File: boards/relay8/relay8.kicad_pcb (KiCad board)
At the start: 2 copper layers, 150 x 95 mm, 56 parts, among them J1 USB-C, J11 CH1, J12 CH2, J13 CH3, J14 CH4, J15 CH5, J16 CH6, J17 CH7, J18 CH8, J2 UART, J3 5V DC 2A, K1 SRD-05VDC-SL-C, K2 SRD-05VDC-SL-C, K3 SRD-05VDC-SL-C, K4 SRD-05VDC-SL-C, K5 SRD-05VDC-SL-C, K6 SRD-05VDC-SL-C, K7 SRD-05VDC-SL-C, K8 SRD-05VDC-SL-C, SW1 RESET, SW2 BOOT, U1 ESP32-C3-WROOM-02-N4, U2 AP2112K-3.3, U3 ULN2803A

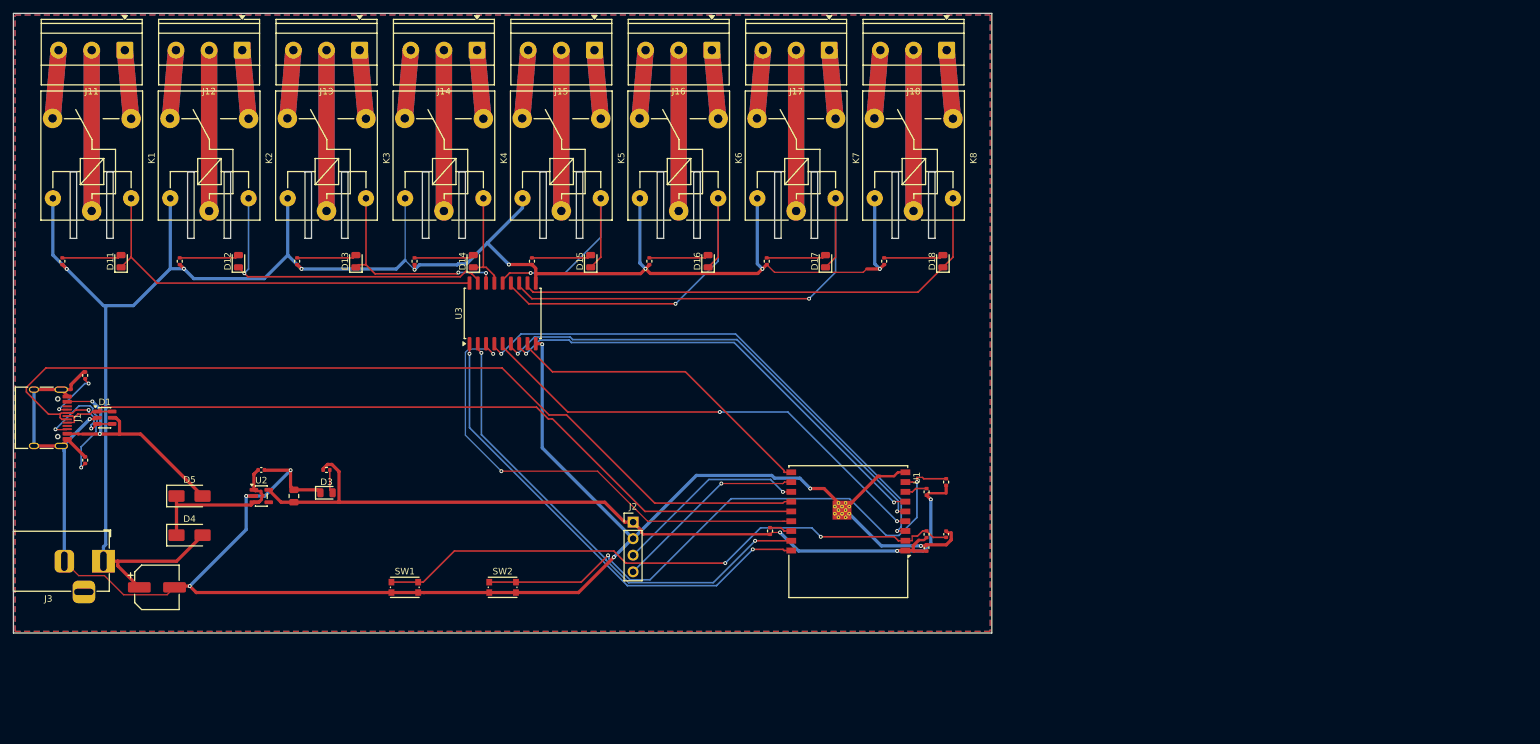
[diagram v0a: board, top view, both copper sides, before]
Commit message: relay8: print NC / COM / NO under every terminal block
The wiring doc said the terminals were labelled, but the board had no
such silkscreen; the only way to tell the contacts apart was the doc.
Each label is generated from the net its pad is on (RL3_NO -> "NO"), so
it cannot disagree with the circuit. Relays, indicator LEDs and the
ULN2803 move down 2.5 mm to make room; the terminal references move to
F.Fab. The 8 silk_overlap warnings are gone as a side effect.

FIRMWARE.md now shows the label order (NC · COM · NO, left to right)
with a rendered close-up and the cut-the-live-wire instruction.
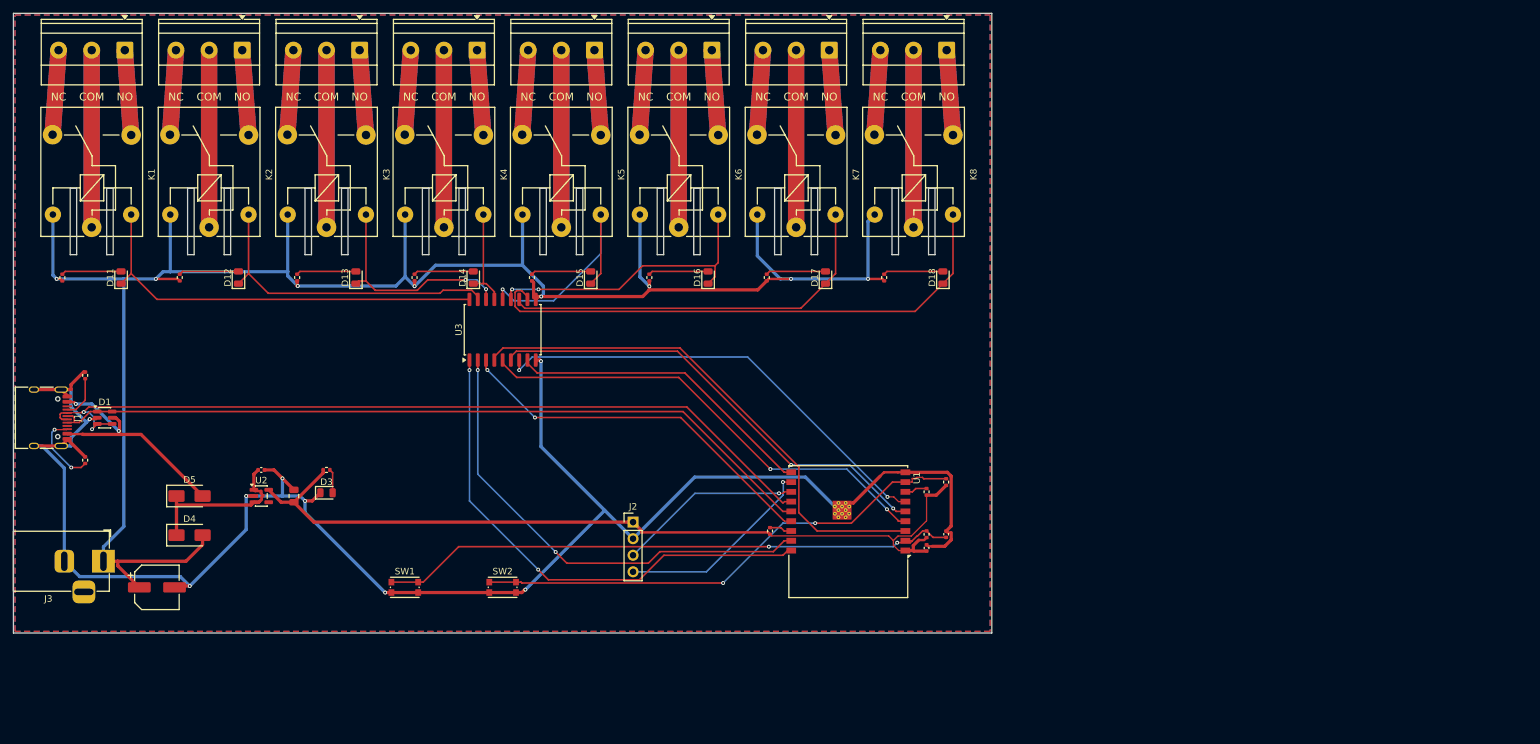
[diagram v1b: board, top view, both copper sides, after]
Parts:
- moved D11 2.50 mm to (116.5, 140.5)
- moved D12 2.50 mm to (134.5, 140.5)
- moved D13 2.50 mm to (152.5, 140.5)
- moved D14 2.50 mm to (170.5, 140.5)
- moved D15 2.50 mm to (188.5, 140.5)
- moved D16 2.50 mm to (206.5, 140.5)
- moved D17 2.50 mm to (224.5, 140.5)
- moved D18 2.50 mm to (242.5, 140.5)
- moved K1 2.50 mm to (112.0, 132.8)
- moved K2 2.50 mm to (130.0, 132.8)
- moved K3 2.50 mm to (148.0, 132.8)
- moved K4 2.50 mm to (166.0, 132.8)
- moved K5 2.50 mm to (184.0, 132.8)
- moved K6 2.50 mm to (202.0, 132.8)
- moved K7 2.50 mm to (220.0, 132.8)
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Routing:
- net USB_DN: track 147.7 -> 127.7 mm
- net IN3: track 74.9 -> 57.8 mm
- net RLY7: track 74.0 -> 60.6 mm, vias 1 -> 0
- net IO9: track 90.2 -> 77.2 mm
- net RLY6: track 56.9 -> 45.4 mm, vias 1 -> 2
- net GND: track 300.8 -> 289.7 mm
- net CC2: track 20.4 -> 11.6 mm
- net RLY8: track 77.4 -> 83.9 mm
- net RL8_COM: track 49.3 -> 54.3 mm
- net RL7_COM: track 49.3 -> 54.3 mm
- net RL6_COM: track 49.3 -> 54.3 mm
- net RL5_COM: track 49.3 -> 54.3 mm
- net RL4_COM: track 49.3 -> 54.3 mm
- net RL3_COM: track 49.3 -> 54.3 mm
- net RL2_COM: track 49.3 -> 54.3 mm
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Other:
- outline, holes or cut-outs redrawn
- board text added: "COM"
- board text added: "NC"
- board text added: "NO"

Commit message: relay8 v2: one mains cable powers everything
The board now takes mains on a single L/N input (J20) instead of a
5 V DC jack plus per-channel feeds:

- J20 -> F1 (T8A, 5x20) -> L bus -> COM of all 8 relays
- N bus from J20 to the middle pin of every output terminal, so each
  appliance connects live and neutral at one terminal: NC . N . NO
- RV1 14D431K across L/N after the fuse
- F2 (T1A, TR5) -> HLK-10M05 (100-240 VAC -> 5 V 2 A) for the relay
  coils and, through the existing diode-OR, the 3.3 V logic

Both buses run on B.Cu (6.5 mm); NO/NC cross them on F.Cu (3.5 mm),
so the layers are separated by the laminate. The F1 exit feeds the L
bus directly and F2 is tapped with a thin trace: routing the bus
through F2's pad left 2.33 mm to F2's other pin (TR5 pitch is 5.1 mm).
Ratings: 5 A per channel, 8 A total. MetzConnect Type171 7.5 mm
terminals; their wire-entry side is not verifiable from KiCad's files
and is listed as a pre-order check.

ERC 0, netlist check 211/211 pins, DRC errors 0, unconnected 0,
schematic parity; 40 silkscreen-clipped-by-slot/edge warnings.
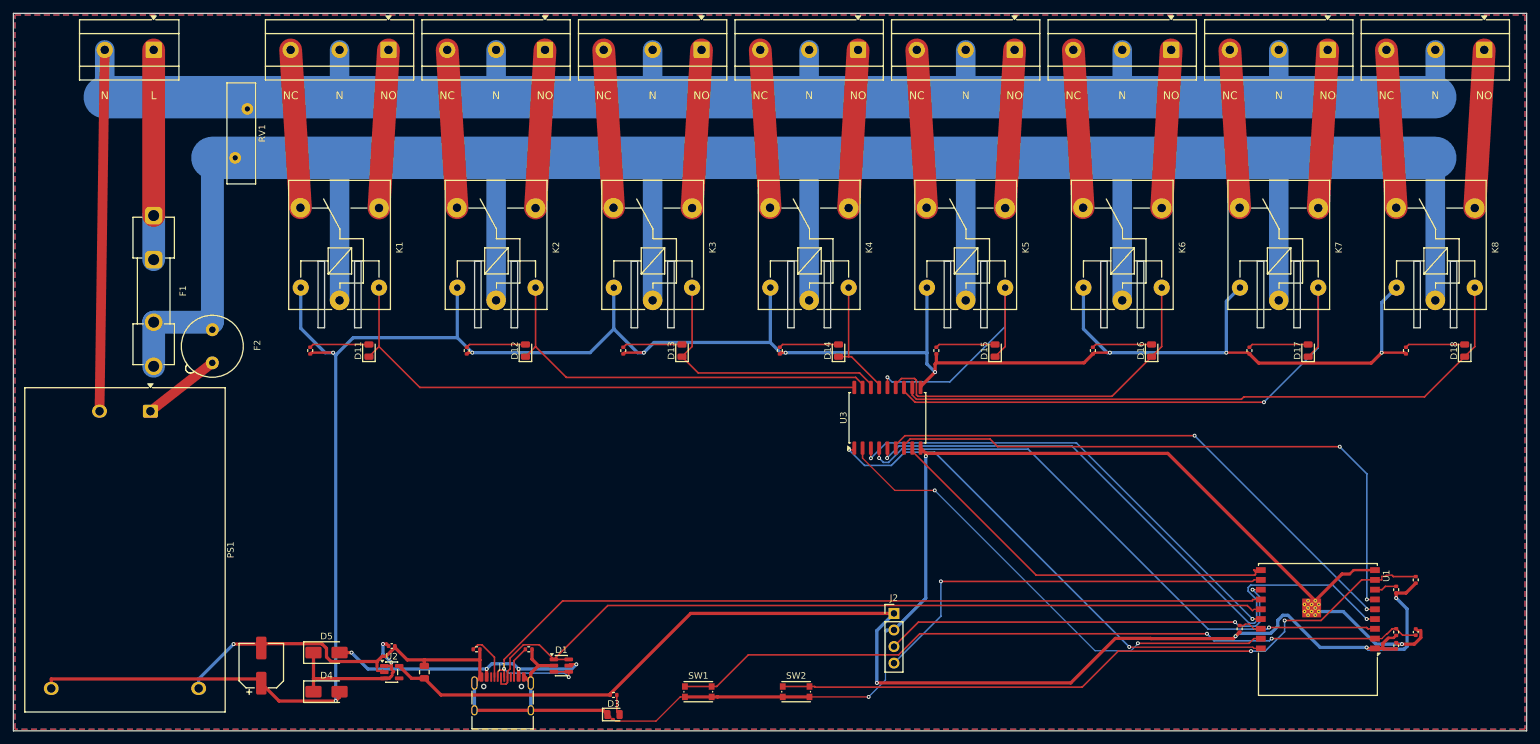
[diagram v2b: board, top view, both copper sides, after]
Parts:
- removed J3: 5V DC 2A, Connector_BarrelJack:BarrelJack_Horizontal
- added F1: T8A 250V, Fuse:Fuseholder_Clip-5x20mm_Keystone_3517_Inline_P23.11x6.76mm_D1.70mm_Horizontal, F.Cu at (121.5, 131.0)
- added F2: T1A 250V, Fuse:Fuseholder_TR5_Littelfuse_No560_No460, F.Cu at (130.5, 148.5)
- added J20: MAINS IN, TerminalBlock_MetzConnect:TerminalBlock_MetzConnect_Type171_RT13702HBWC_1x02_P7.50mm_Horizontal, F.Cu at (121.5, 105.6)
- added PS1: HLK-10M05, Converter_ACDC:Converter_ACDC_Hi-Link_HLK-10Mxx, F.Cu at (121.0, 161.0)
- added RV1: 14D431K, Varistor:RV_Disc_D15.5mm_W4.4mm_P7.5mm, F.Cu at (134.0, 122.2)
- J11, J12, J13, J14, J15, J16, J17, J18: footprint TerminalBlock_Phoenix:TerminalBlock_Phoenix_MKDS-1,5-3-5.08_1x03_P5.08mm_Horizontal -> TerminalBlock_MetzConnect:TerminalBlock_MetzConnect_Type171_RT13703HBWC_1x03_P7.50mm_Horizontal
- moved J1 83.3 mm to (175.0, 205.8), turned to 0 degrees
- moved J18 82.4 mm to (325.5, 105.6)
- moved D18 80.8 mm to (322.5, 151.7)
- moved K8 80.8 mm to (318.0, 144.0)
- moved R18 80.8 mm to (313.5, 151.7)
- moved D1 79.6 mm to (184.0, 200.0)
- moved J17 76.4 mm to (301.5, 105.6)
- moved D17 74.8 mm to (298.5, 151.7)
- moved K7 74.8 mm to (294.0, 144.0)
- moved R17 74.8 mm to (289.5, 151.7)
- moved R2 73.9 mm to (179.0, 197.5), turned to 0 degrees
- moved C3 73.5 mm to (312.0, 197.0)
- moved C4 73.5 mm to (315.0, 194.9)
- moved R3 73.5 mm to (312.0, 194.9)
- moved R4 73.5 mm to (315.0, 186.9)
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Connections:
- net DC_IN renamed 5V_PS
- J11 pad 2: RL1_COM -> N_BUS
- J12 pad 2: RL2_COM -> N_BUS
- J13 pad 2: RL3_COM -> N_BUS
- J14 pad 2: RL4_COM -> N_BUS
- J15 pad 2: RL5_COM -> N_BUS
- J16 pad 2: RL6_COM -> N_BUS
- J17 pad 2: RL7_COM -> N_BUS
- J18 pad 2: RL8_COM -> N_BUS
- K1 pad 1: RL1_COM -> L_BUS
- K2 pad 1: RL2_COM -> L_BUS
- K3 pad 1: RL3_COM -> L_BUS
- K4 pad 1: RL4_COM -> L_BUS
- K5 pad 1: RL5_COM -> L_BUS
- K6 pad 1: RL6_COM -> L_BUS
- K7 pad 1: RL7_COM -> L_BUS
- K8 pad 1: RL8_COM -> L_BUS
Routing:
- net L_BUS: track 0.00 -> 404.4 mm
- net N_BUS: track 0.00 -> 324.7 mm
- net +3V3: track 129.3 -> 204.5 mm, vias 0 -> 4
- net 5V_PS: track 295.2 -> 369.9 mm, vias 8 -> 9
- net RL8_COM: track 54.3 -> 0.00 mm
- net RL7_COM: track 54.3 -> 0.00 mm
- net RL6_COM: track 54.3 -> 0.00 mm
- net RL5_COM: track 54.3 -> 0.00 mm
- net RL4_COM: track 54.3 -> 0.00 mm
- net RL3_COM: track 54.3 -> 0.00 mm
- net RL2_COM: track 54.3 -> 0.00 mm
- net RL1_COM: track 54.3 -> 0.00 mm
- net TXD: track 28.3 -> 64.8 mm, vias 1 -> 2
- net RXD: track 31.2 -> 64.7 mm
- net L_IN: track 0.00 -> 32.2 mm
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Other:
- board size 150 x 95 mm -> 232 x 110 mm
- board text added: "L"
- board text added: "N"
- board text removed: "COM"

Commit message: esp32c3, relay8: LP38693 instead of AP2112K (hot-plug overshoot exceeded 6.5 V)
With only 1 uF on VBUS, cable ringing on hot-plug reaches 8.6 V (esp32c3) and
7.7 V (relay8, through SS34) at the LDO input; AP2112K's absolute maximum is
6.5 V. The USBLC6 VBUS zener lowers it by ~0.6 V, not enough. LP38693 is rated
12 V. New boards/esp32c3/sim/power_sim.py covers both boards and includes the
module's own ~12.3 uF (WROOM-02 datasheet fig. 8-1): total hot-plug charge is
~79 uC, over USB 2.0's 50 uC; documented as a compliance limitation.
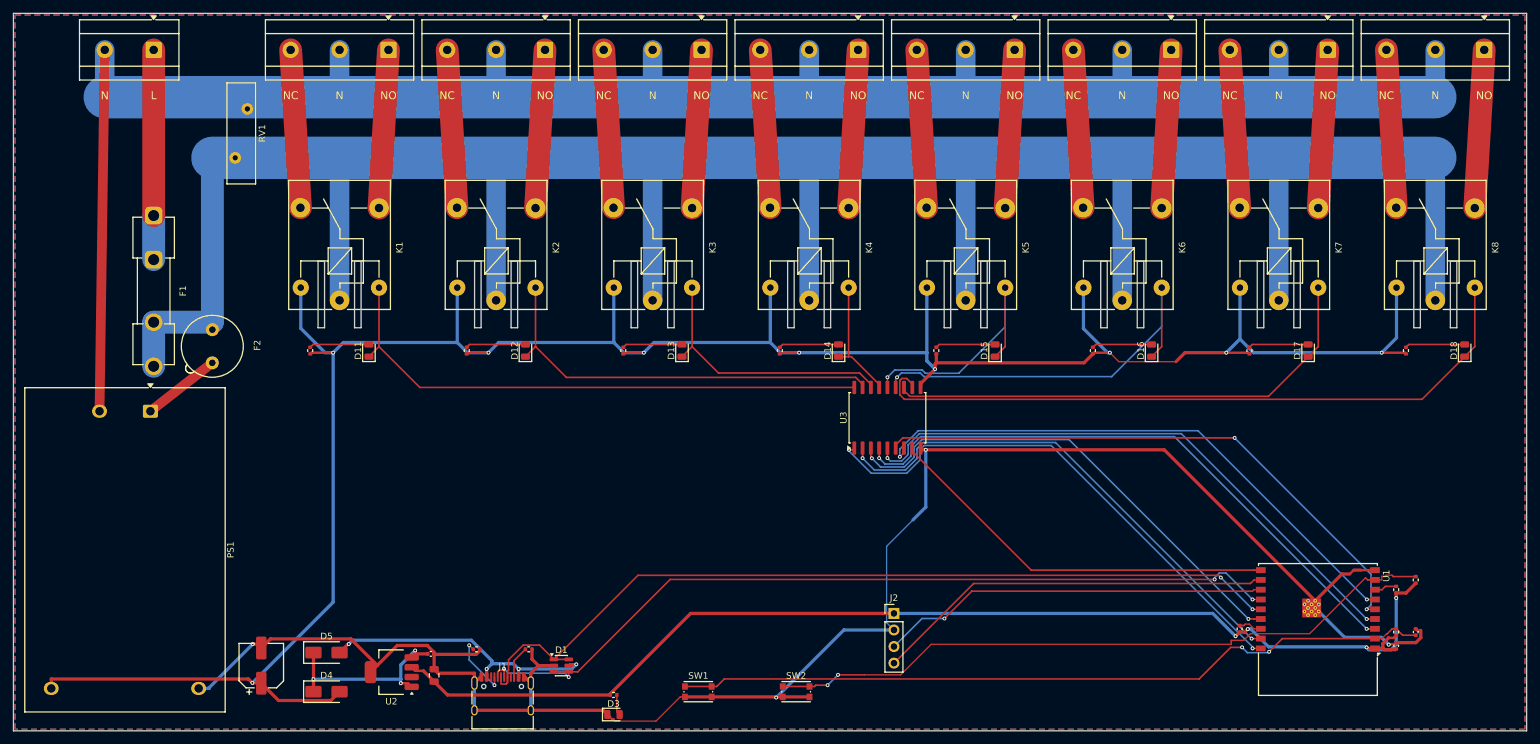
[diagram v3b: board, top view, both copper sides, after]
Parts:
- U2: value AP2112K-3.3 -> LP38693MP-3.3; footprint Package_TO_SOT_SMD:SOT-23-5 -> Package_TO_SOT_SMD:SOT-223-5
- moved C1 6.12 mm to (164.0, 198.2)
- moved C2 1.58 mm to (164.5, 201.5)
- turned U2 to 180 degrees
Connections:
- U2 pad 2: GND -> unconnected-(U2-NC-Pad2)
- U2 pad 3: 5V_SYS -> +3V3
- U2 pad 4: unconnected-(U2-NC-Pad4) -> 5V_SYS
- U2 pad 5: +3V3 -> GND
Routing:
- net +3V3: track 204.5 -> 181.1 mm
- net RLY7: track 88.7 -> 76.5 mm, vias 1 -> 0
- net 5V_PS: track 369.9 -> 378.6 mm
- net USB_DN: track 138.1 -> 131.0 mm, vias 2 -> 4
- net IN7: track 94.5 -> 87.5 mm
- net IN5: track 97.8 -> 90.8 mm
- net RLY6: track 56.3 -> 63.1 mm, vias 0 -> 1
- net RLY8: track 100.1 -> 105.9 mm
- net GND: track 294.3 -> 299.4 mm
- net TXD: track 64.8 -> 59.9 mm, vias 2 -> 1
- net 5V_SYS: track 26.0 -> 30.4 mm, vias 2 -> 3
- net IN6: track 85.7 -> 89.4 mm
- net USB_DP: track 129.1 -> 132.7 mm, vias 0 -> 2
- net RXD: track 64.7 -> 61.5 mm, vias 1 -> 0
- net IN1: track 78.4 -> 81.4 mm
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
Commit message: fab: Gerber/drill zip + JLCPCB BOM/CPL with self-checks; USBLC6-2SC6 to match SOT-23-6
lib/fab.py runs as the last build step on all three boards. It refuses to
write the zip when a required Gerber layer is missing or empty, when the
drill-hit count differs from vias + plated/NPTH pad holes (route-format
slots counted once), or when BOM / CPL / board refdes sets disagree.

It also compares each symbol's library default footprint with the one
actually assigned. That caught all three boards using the USBLC6-2P6
symbol (SOT-666) on a SOT-23-6 footprint: electrically identical pinout,
so ERC/DRC/netlist checks passed, but a BOM ordered by value would buy a
part that does not fit. Switched to USBLC6-2SC6.

LCSC part numbers come from a hand-checked boards/<b>/lcsc.json; the
script never guesses them and lists missing rows in fab/missing-lcsc.txt.
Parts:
- D1: value USBLC6-2P6 -> USBLC6-2SC6
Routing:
- net IN1: track 81.4 -> 98.2 mm
- net VBUS: track 44.3 -> 57.8 mm, vias 4 -> 3
- net 5V_PS: track 378.6 -> 367.7 mm
- net RLY7: track 76.5 -> 86.3 mm, vias 0 -> 1
- net IN3: track 75.8 -> 84.9 mm
- net IN2: track 78.4 -> 85.3 mm
- net RLY8: track 105.9 -> 100.0 mm
- net RLY6: track 63.1 -> 57.4 mm, vias 1 -> 0
- net EN: track 116.8 -> 121.8 mm
- net IN4: track 92.8 -> 96.6 mm
- net USB_DN: track 131.0 -> 134.8 mm, vias 4 -> 2
- net USB_DP: track 132.7 -> 129.0 mm, vias 2 -> 0
- net IN5: track 90.8 -> 94.2 mm
- net IN7: track 87.5 -> 89.3 mm
- net RLY3: track 41.5 -> 42.4 mm
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
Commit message: fab: verified LCSC part numbers for all three boards; BOM/CPL ready to upload
lib/lcsc.py checks every hand-written part number in boards/<b>/lcsc.json
against the JLCPCB parts API: the part exists, its model equals the one
written down, stock covers 5 boards, the package matches what the KiCad
footprint name implies (0402/0805, SOT-23(-6), SOT-223-5, SMA, SOIC-W,
CP_Elec, 2.54 mm headers), resistor/capacitor values match the JLC
attributes and LED colours match. A mutation test (1k part for a 10k
resistor, wrong model, 0805 part on a 0402 footprint, missing row) fails
all four. Results go to lcsc-check.json with a hash of lcsc.json, so the
build itself stays offline and refuses a stale check.

fab.py now writes BOM/CPL only for assembled parts, lists parts LCSC
cannot supply in hand-solder.csv (relay8: mains terminals and fuse
holders), applies lib/jlc_rotations.json to the CPL and writes
rotation-review.csv. None of the rotation corrections are verified on
hardware; every row says so.
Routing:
- net IN1: track 98.2 -> 79.7 mm
- net VBUS: track 57.8 -> 46.8 mm, vias 3 -> 2
- net IN3: track 84.9 -> 74.7 mm
- net RLY7: track 86.3 -> 77.0 mm, vias 1 -> 0
- net IN8: track 61.5 -> 70.4 mm, vias 0 -> 2
- net IN2: track 85.3 -> 77.1 mm
- net 5V_PS: track 367.7 -> 375.7 mm
- net USB_DN: track 134.8 -> 128.2 mm
- net IN5: track 94.2 -> 100.7 mm, vias 2 -> 0
- net RLY8: track 100.0 -> 106.3 mm
- net IO9: track 105.8 -> 112.0 mm
- net IN4: track 96.6 -> 91.4 mm
- net GND: track 299.3 -> 303.8 mm, vias 4 -> 5
- net USB_DP: track 129.0 -> 125.0 mm, vias 0 -> 4
- net TXD: track 59.9 -> 63.8 mm
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
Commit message: review: datasheet design review on the netlist; fixes a reversed TVS and dim LEDs
lib/review.py checks the design intent that ERC and the netlist check take
on trust: diode/TVS polarity against inferred rail voltages, LED current
from the JLC Vf range, per-datasheet decoupling and supply ranges, USB-C
CC pull-downs and D+/D- on both sides, ESP32-C3 EN RC, strapping pins and
GPIO18/19, relay flyback path and pickup voltage, capacitor rating and
polarity. It runs after the netlist check and stops the build on ERROR.
lib/review_test.py breaks the real netlists 15 ways; every rule fires and
the unmodified boards report no ERROR.

Real defects it found:
- usbc-ldo: SMAJ5.0A had anode on +5V and cathode on GND (KiCad names
  the cathode pin "A1"), shorting the rail on plug-in. Swapped.
- esp32c3: blue user LED on a 3.3 V GPIO (Vf 2.5-3.6 V) -> yellow, 470R.
- esp32c3, relay8: green power LED at ~0.45 mA through 1k -> 220R.
- usbc-ldo: SS32 symbol for an SS34 part -> Diode:SS34.

Also: lcsc-check.json keeps JLC attributes (Vf, voltage rating) for the
review; lcsc.py groups parts from net.txt instead of fab/groups.json; the
build retries freerouting (up to 3 runs) because it is not deterministic
and occasionally leaves two connections unrouted on the same DSN.
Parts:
- R8: value 1k -> 220
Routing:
- net IN5: track 100.7 -> 88.8 mm, vias 0 -> 2
- net RLY7: track 77.0 -> 88.8 mm, vias 0 -> 1
- net USB_DN: track 128.2 -> 139.5 mm
- net IN8: track 70.4 -> 61.5 mm, vias 2 -> 0
- net IN1: track 79.7 -> 88.4 mm
- net IN3: track 74.7 -> 81.6 mm
- net 5V_PS: track 375.7 -> 369.3 mm, vias 9 -> 10
- net RLY8: track 106.3 -> 100.1 mm
- net TXD: track 63.8 -> 59.9 mm, vias 2 -> 1
- net GND: track 303.8 -> 300.3 mm
- net USB_DP: track 125.0 -> 127.5 mm, vias 4 -> 0
- net VBUS: track 46.8 -> 44.4 mm, vias 2 -> 4
- net +3V3: track 183.2 -> 185.4 mm, vias 2 -> 3
- net EN: track 118.1 -> 116.1 mm, vias 2 -> 0
- net RLY5: track 40.6 -> 42.3 mm
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
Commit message: build: reproducible output (seeded UUIDs, single-thread freerouting, no retry)
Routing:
- net VBUS: track 44.4 -> 56.0 mm
- net IN1: track 88.4 -> 76.8 mm
- net IN3: track 81.6 -> 71.3 mm
- net GND: track 300.3 -> 310.5 mm
- net IN7: track 92.8 -> 82.7 mm
- net TXD: track 59.9 -> 69.9 mm
- net +3V3: track 185.4 -> 175.5 mm, vias 3 -> 4
- net RLY5: track 42.3 -> 32.8 mm
- net RXD: track 61.5 -> 67.2 mm
- net USB_DN: track 139.5 -> 134.8 mm
- net IN2: track 77.7 -> 73.4 mm
- net IN5: track 88.8 -> 86.5 mm
- net IN4: track 90.9 -> 88.6 mm
- net 5V_PS: track 369.3 -> 367.2 mm, vias 10 -> 9
- net IN6: track 85.7 -> 87.5 mm
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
